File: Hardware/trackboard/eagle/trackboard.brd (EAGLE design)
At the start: 160 x 100 mm, 29 parts, among them U9.00 ADNS-3080, U9.02 SI1922EDH, X9.00 RESON

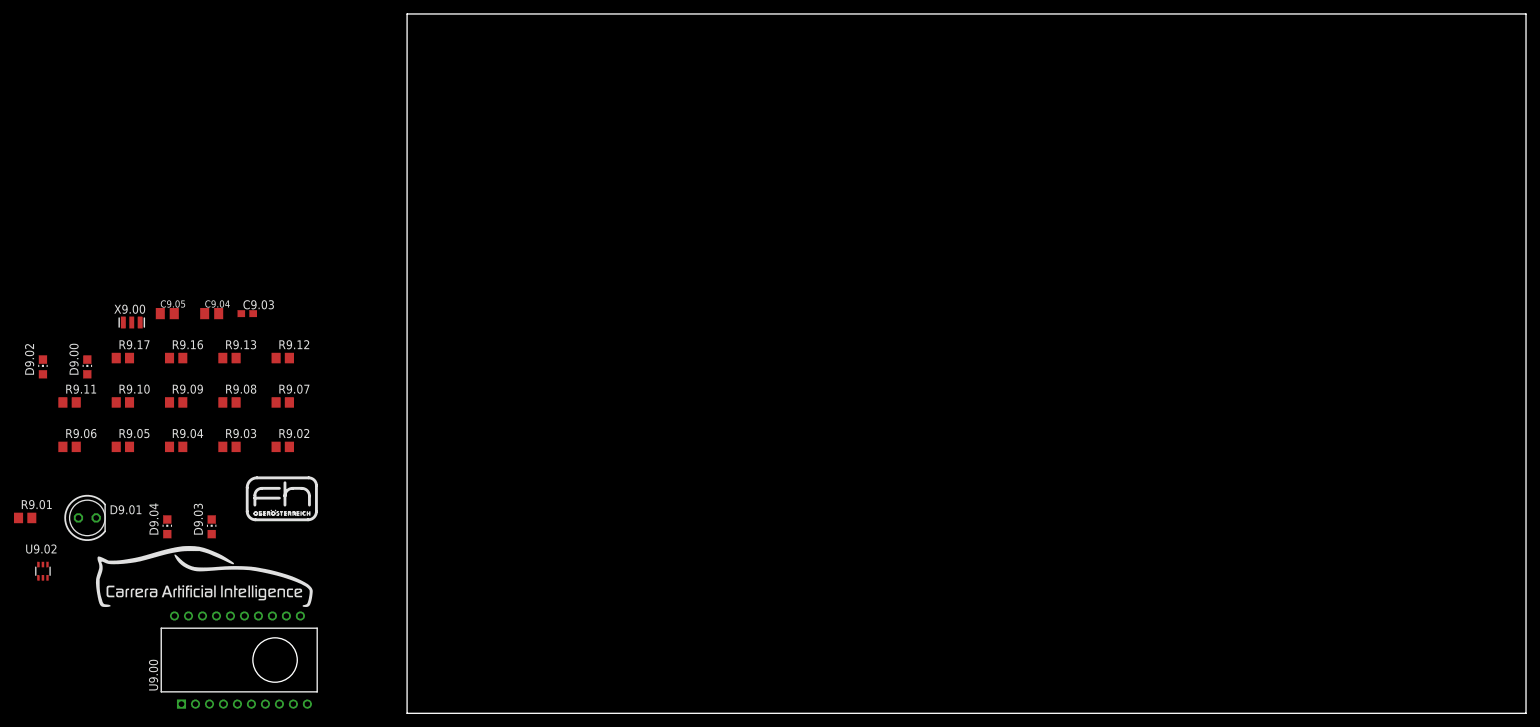
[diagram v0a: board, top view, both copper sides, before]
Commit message: board dimensions fixed ; layed out some traces ; needs clarification on what's allowed regarding cuts through pads
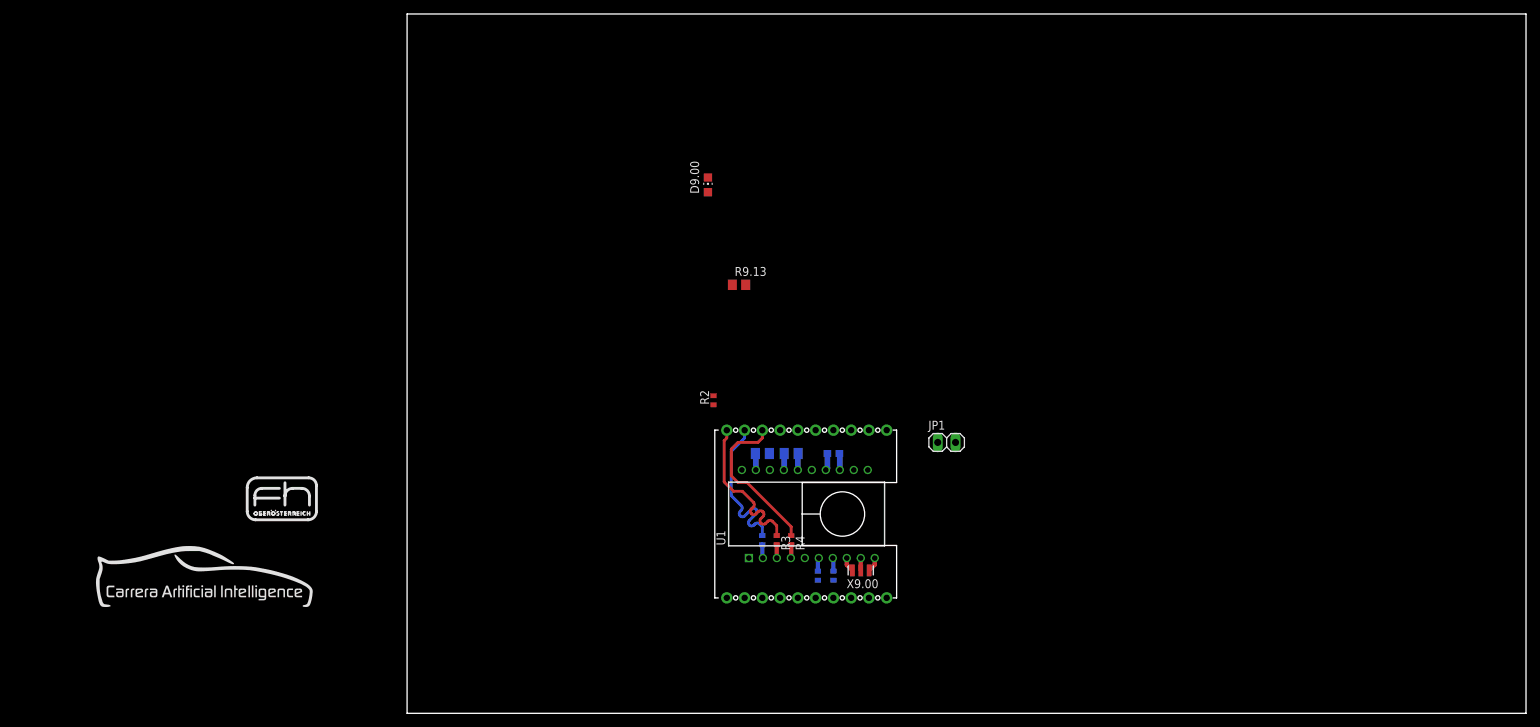
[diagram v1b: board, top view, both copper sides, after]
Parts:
- removed D9.01: RED, led:LED5MM
- removed D9.02: RED, led:CHIP-LED0805
- removed D9.03, D9.04: GREEN, led:CHIP-LED0805
- removed R9.03, R9.04, R9.05: [PPR], rcl:R0805
- removed R9.06, R9.07, R9.11, R9.12: [0R], rcl:R0805
- removed R9.08: 180R, rcl:R0805
- removed R9.09, R9.10: 330R, rcl:R0805
- removed R9.16, R9.17: 10kR, rcl:R0805
- removed U9.00: ADNS-3080, kitt.ic:ADNS-3080
- removed U9.02: SI1922EDH, kitt.ic:SC70-6
- added JP1: (no value), pinhead:1X02
- added R1, R3, R4: 100R, rcl:R0402
- added R2: 10kR, rcl:R0402
- added U1: ADNS-3080, kitt.ic:ADNS-3080
- R9.01, R9.02: value [PPR] -> 10kR; device rcl:R0805 -> rcl:R0402
- moved R9.01 115.9 mm to (61.0, 19.7), flipped to the bottom, turned to 90 degrees
- moved X9.00 110.1 mm to (64.9, 20.4), turned to 180 degrees
- moved DCL2 95.5 mm to (76.3, 29.6)
- moved D9.00 92.5 mm to (43.0, 75.6)
- moved C9.05 87.4 mm to (50.8, 37.1), flipped to the bottom
- moved C9.03 86.2 mm to (61.0, 37.1), flipped to the bottom
- moved C9.04 85.2 mm to (54.9, 37.1), flipped to the bottom, turned to 180 degrees
- moved R9.02 78.7 mm to (58.7, 19.7), flipped to the bottom, turned to 90 degrees
- moved R9.13 73.6 mm to (47.5, 61.3)
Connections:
- removed net !LEDCTRL: R9.07.2, R9.11.1
- removed net AUXLED: R9.12.1
- removed net N$168: R9.02.1, U9.00.1
- removed net N$182: R9.03.1, U9.00.2
- removed net N$183: R9.04.1, U9.00.3
- removed net N$184: R9.11.2, R9.12.2, R9.16.1, U9.02.5
- removed net N$185: D9.04.C, R9.10.2
- removed net N$186: R9.09.1, R9.10.1, U9.02.3
- removed net N$187: D9.03.C, R9.09.2
- removed net N$188: R9.05.1, U9.00.4
- removed net N$4: R9.06.2, R9.07.1, R9.17.1, U9.00.5, U9.02.2
- removed net N$8: D9.01.K, D9.02.C, R9.08.2
- new net U1.MISO: R1.2, U1.2
- new net U1.MOSI: R4.2, U1.4
- new net U1.SCLK: R3.2, U1.3
- net !CS: now also R2.2, U1.1; no longer R9.02.2
- net !PD: now also U1.7; no longer U9.00.7
- net +3V3: now also R2.1, R9.02.1, U1.12, U1.15, U1.17; no longer D9.01.A, D9.02.A, D9.03.A, D9.04.A, U9.00.12, U9.00.15, U9.00.17
- net GND: now also U1.16, U1.19; no longer R9.16.2, R9.17.2, U9.00.16, U9.00.19, U9.02.1, U9.02.4
- net MISO: now also R1.1; no longer R9.03.2
- net MOSI: now also R4.1; no longer R9.05.2
- net N$1: now also U1.9; no longer U9.00.9
- net N$2: now also U1.8; no longer U9.00.8
- net N$3: now also U1.10; no longer U9.00.10
- net N$5: now also U1.13; no longer U9.00.13
- net N$6: now also U1.14; no longer U9.00.14
- net N$7: now also JP1.1, U1.5; no longer R9.06.1, R9.08.1, U9.02.6
- net RST: now also R9.02.2, U1.6; no longer U9.00.6
- net SCLK: now also R3.1; no longer R9.04.2
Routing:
- net MOSI: track 0.00 -> 22.9 mm, vias 0 -> 1
- net SCLK: track 0.00 -> 22.5 mm, vias 0 -> 1
- net MISO: track 0.00 -> 22.3 mm, vias 0 -> 1
- net GND: track 0.00 -> 4.82 mm
- net N$6: track 0.00 -> 2.45 mm
- net N$5: track 0.00 -> 2.37 mm
- net +3V3: track 0.00 -> 2.37 mm
- net N$3: track 0.00 -> 2.10 mm
- net N$2: track 0.00 -> 2.09 mm
- net U1.MISO: track 0.00 -> 2.05 mm
- net RST: track 0.00 -> 1.92 mm
- net U1.SCLK: track 0.00 -> 1.92 mm
- net U1.MOSI: track 0.00 -> 1.91 mm
- net !PD: track 0.00 -> 1.90 mm
- net N$1: track 0.00 -> 1.76 mm
- added copper zone on layer 2, net GND
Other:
- outline, holes or cut-outs redrawn

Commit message: ADNS3080 module is pretty much okay now ; will be imported into correct place in baseboard
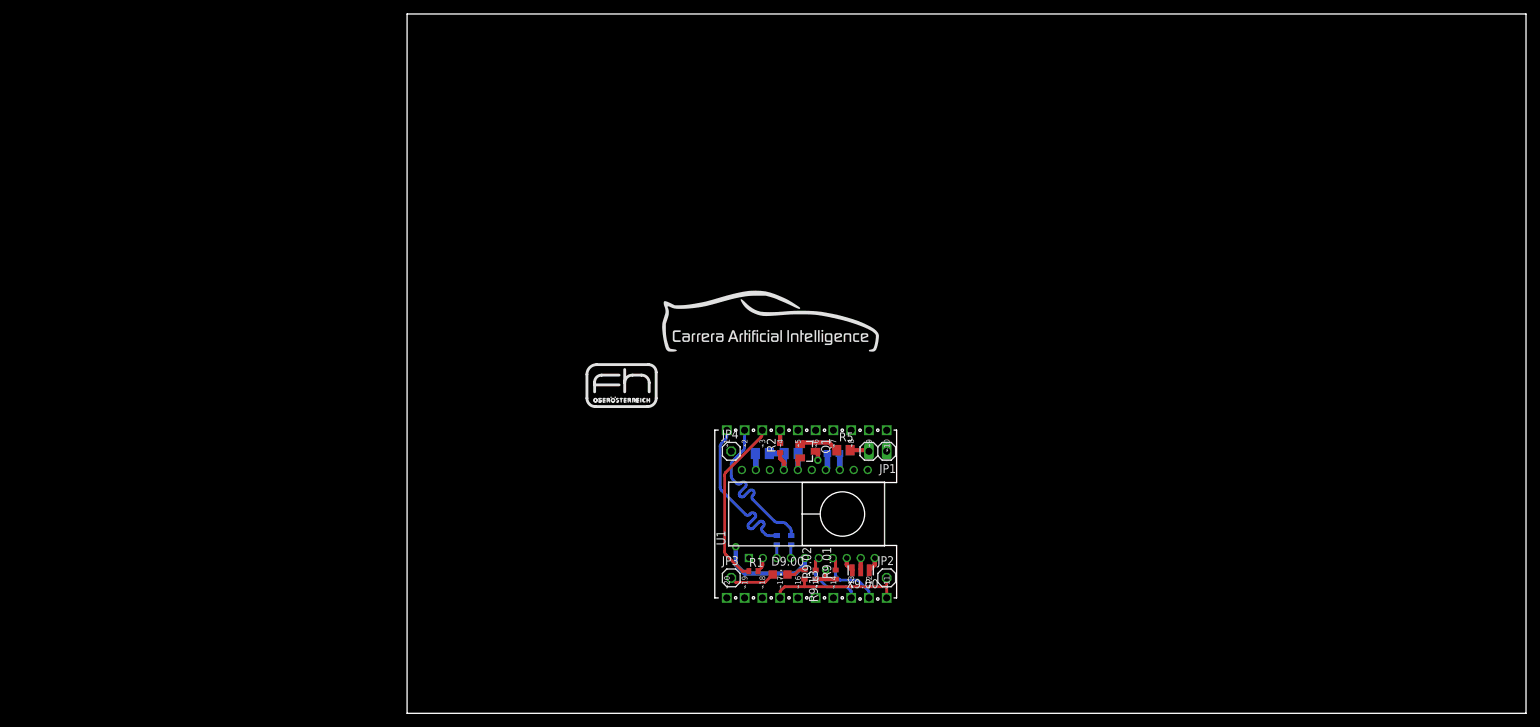
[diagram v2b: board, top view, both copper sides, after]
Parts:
- added JP2, JP3, JP4: (no value), pinhead:1X01
- added Q1: BS170, transistor-fet:SOT23
- added R5: (no value), rcl:R0805
- added ⌁1, ⌁10, ⌁11, ⌁12, ⌁13, ⌁14, ⌁15, ⌁16, ⌁17, ⌁18, ⌁19, ⌁2, ⌁20, ⌁3, ⌁4, ⌁5, ⌁6, ⌁7, ⌁8, ⌁9: SINGLEPAD40MIL, kitt.con:PAD40MIL
- R9.13: device rcl:R0805 -> rcl:R0402
- moved DCL1 88.8 mm to (51.8, 54.3)
- moved D9.00 56.7 mm to (53.3, 19.8), turned to 270 degrees
- moved REF1 51.2 mm to (25.7, 42.9)
- moved R9.13 42.5 mm to (56.8, 19.8), turned to 270 degrees
- moved DCL2 22.7 mm to (53.6, 30.7), flipped to the bottom
- moved R2 11.7 mm to (53.3, 37.9)
- moved JP1 9.92 mm to (67.3, 37.5), turned to 180 degrees
- moved R1 4.62 mm to (49.5, 20.3), flipped to the top, turned to 0 degrees
- moved R9.01 0.35 mm to (61.3, 19.8), flipped to the top
- moved R9.02 0.35 mm to (58.4, 19.8), flipped to the top
- flipped R3 to the bottom
- flipped R4 to the bottom
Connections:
- removed net !CS: R2.2, U1.1
- new net !CS0: R2.2, U1.1, ⌁4.X
- new net !CS1: ⌁5.X
- new net !INT: ⌁6.X
- new net GPIO1: ⌁14.X
- new net GPIO2: ⌁15.X
- new net GPIO3: ⌁16.X
- new net N$4: Q1.3, U1.5
- new net N$8: JP1.2, R5.2
- new net N$9: U1.20
- new net SCL: ⌁8.X
- new net SDA: ⌁7.X
- new net V++: ⌁20.X
- net !PD: now also ⌁12.X
- net +3V3: now also JP1.1, JP3.1, ⌁10.X
- net GND: now also JP2.1, JP4.1, Q1.2, ⌁11.X, ⌁17.X, ⌁9.X
- net MISO: now also ⌁3.X
- net MOSI: now also ⌁2.X
- net N$7: now also Q1.1, R5.1; no longer JP1.1, U1.5
- net RST: now also ⌁13.X
- net SCLK: now also ⌁1.X
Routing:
- net N$4: track 0.00 -> 42.5 mm, vias 1 -> 2
- net !CS0: track 0.00 -> 31.5 mm
- net GND: track 4.82 -> 29.9 mm
- net +3V3: track 2.37 -> 18.1 mm, vias 0 -> 1
- net RST: track 1.92 -> 11.6 mm
- net !PD: track 1.90 -> 11.2 mm
- net N$7: track 0.00 -> 5.82 mm
- net N$8: track 0.00 -> 2.77 mm, vias 1 -> 0
- net N$11: track 0.00 -> 2.71 mm
- net MISO: track 22.3 -> 24.3 mm, vias 1 -> 0
- net SCLK: track 22.5 -> 23.8 mm, vias 1 -> 0
- net MOSI: track 22.9 -> 23.8 mm, vias 1 -> 0
- added copper zone on layer 15, net +3V3
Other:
- outline, holes or cut-outs redrawn
